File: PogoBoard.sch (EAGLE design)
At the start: 4 parts

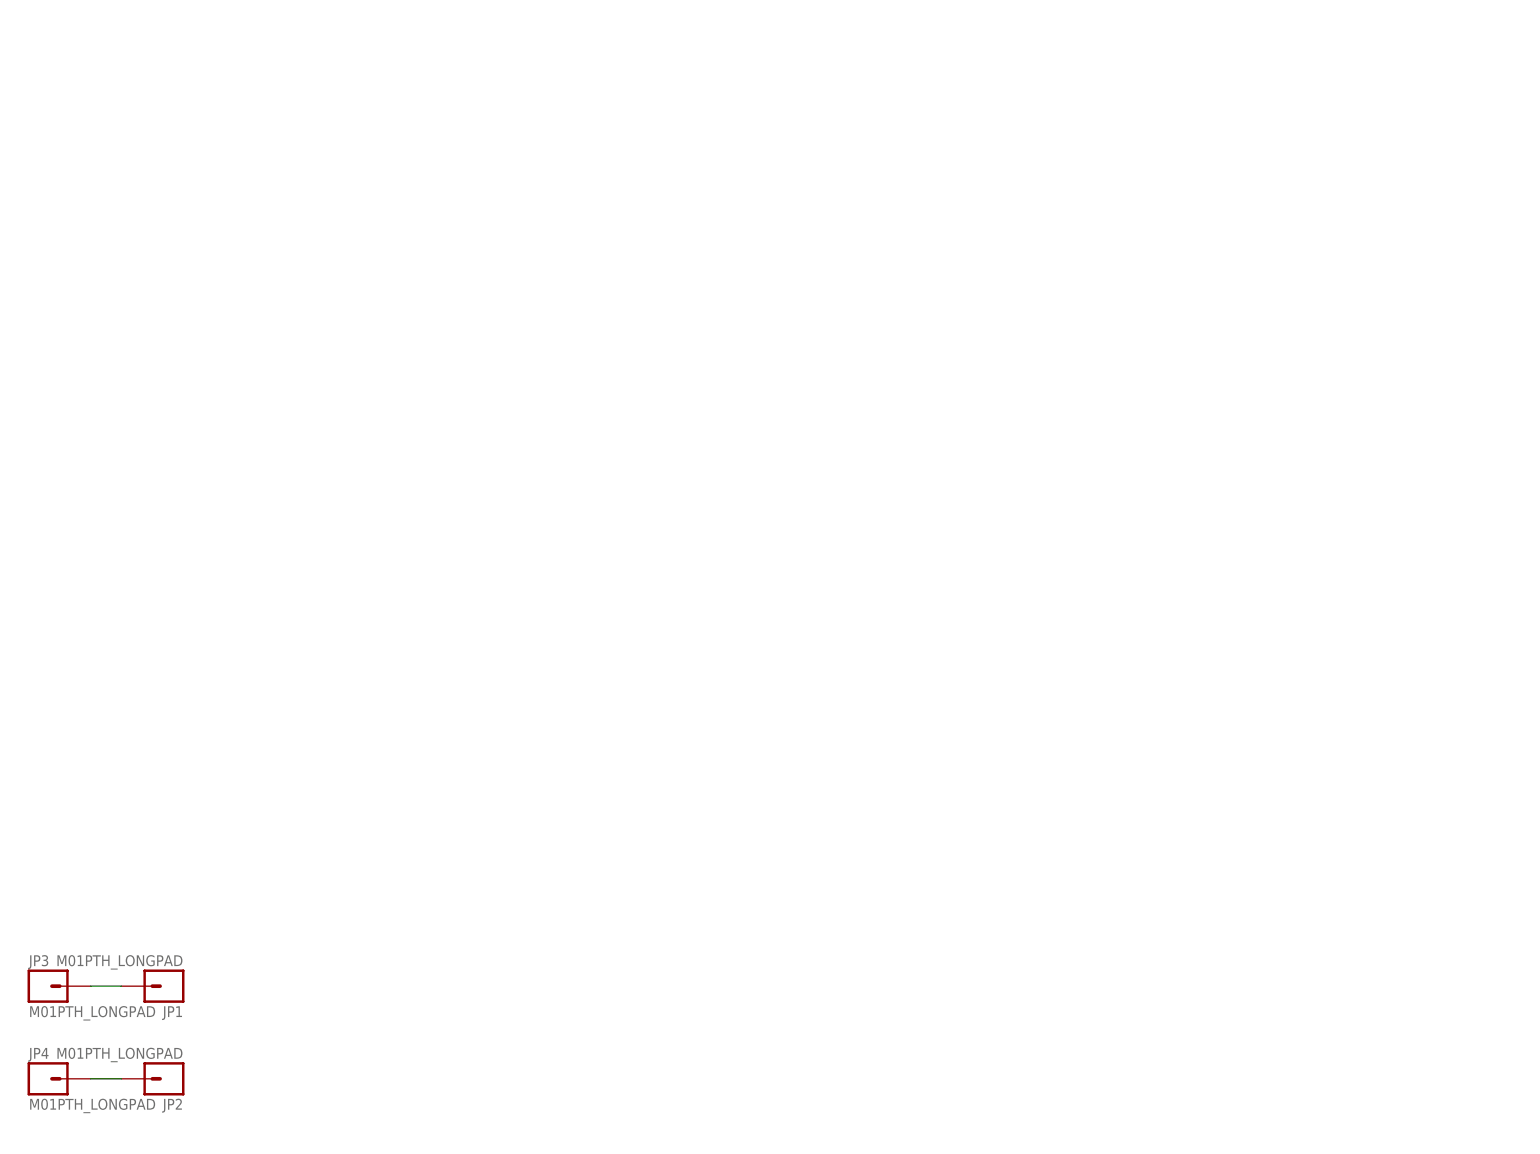
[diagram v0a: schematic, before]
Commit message: Changed pogo board screws to M3
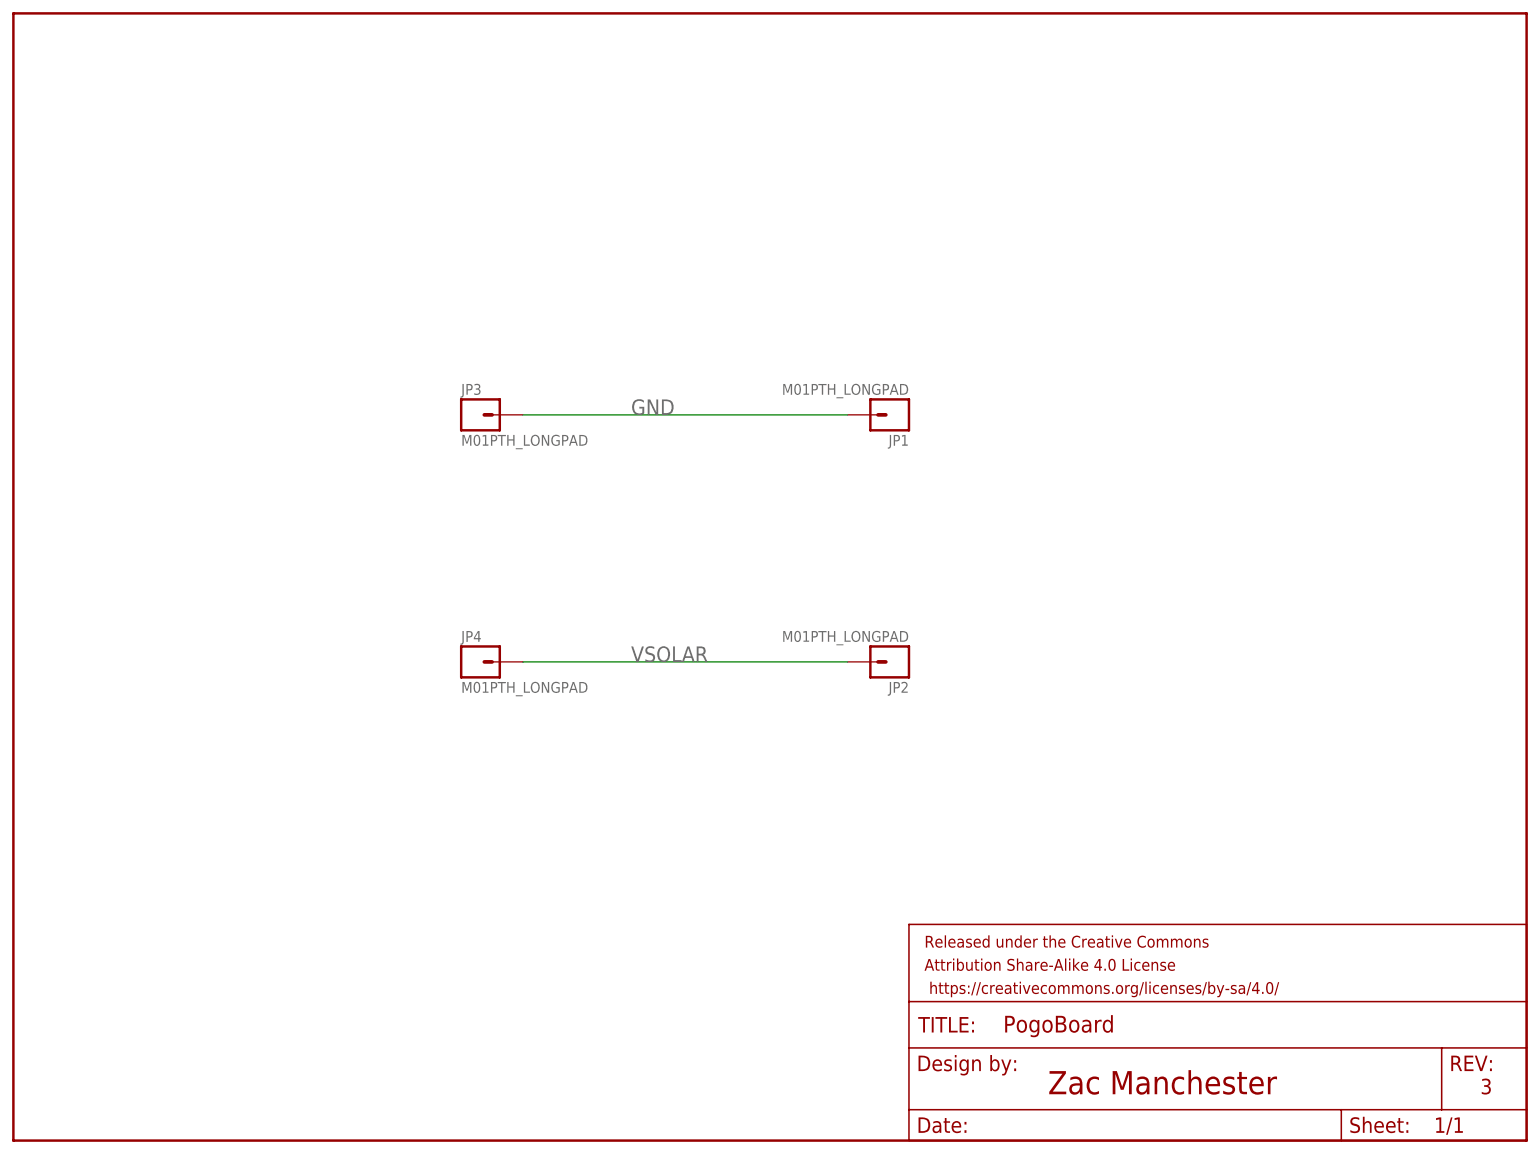
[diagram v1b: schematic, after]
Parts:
- added FRAME1: FRAME-LETTER, SparkFun-Aesthetics:FRAME-LETTER
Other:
- note added: "3"
- note added: "Zac Manchester"
- moved on the sheet: JP1, JP2, JP3, JP4
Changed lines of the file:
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@@
 <layer number="106" name="bPlate" color="7" fill="1" visible="yes" active="yes"/>
 <layer number="107" name="Crop" color="7" fill="1" visible="yes" active="yes"/>
+<layer number="108" name="tplace-old" color="10" fill="1" visible="no" active="yes"/>
+<layer number="109" name="ref-old" color="11" fill="1" visible="no" active="yes"/>
 <layer number="116" name="Patch_BOT" color="9" fill="4" visible="yes" active="yes"/>
 <layer number="121" name="_tsilk" color="7" fill="1" visible="yes" active="yes"/>
 <layer number="122" name="_bsilk" color="7" fill="1" visible="yes" active="yes"/>
+<layer number="125" name="_tNames" color="7" fill="1" visible="yes" active="yes"/>
 <layer number="144" name="Drill_legend" color="7" fill="1" visible="yes" active="yes"/>
 <layer number="151" name="HeatSink" color="7" fill="1" visible="yes" active="yes"/>
+<layer number="199" name="Contour" color="7" fill="1" visible="yes" active="yes"/>
 <layer number="200" name="200bmp" color="1" fill="10" visible="yes" active="yes"/>
 <layer number="201" name="201bmp" color="2" fill="10" visible="yes" active="yes"/>
@@
 <layer number="215" name="215bmp" color="7" fill="1" visible="yes" active="yes"/>
 <layer number="216" name="216bmp" color="7" fill="1" visible="yes" active="yes"/>
+<layer number="217" name="217bmp" color="18" fill="1" visible="no" active="no"/>
+<layer number="218" name="218bmp" color="19" fill="1" visible="no" active="no"/>
+<layer number="219" name="219bmp" color="20" fill="1" visible="no" active="no"/>
+<layer number="220" name="220bmp" color="21" fill="1" visible="no" active="no"/>
+<layer number="221" name="221bmp" color="22" fill="1" visible="no" active="no"/>
+<layer number="222" name="222bmp" color="23" fill="1" visible="no" active="no"/>
+<layer number="223" name="223bmp" color="24" fill="1" visible="no" active="no"/>
+<layer number="224" name="224bmp" color="25" fill="1" visible="no" active="no"/>
 <layer number="250" name="Descript" color="3" fill="1" visible="no" active="no"/>
 <layer number="251" name="SMDround" color="12" fill="11" visible="no" active="no"/>
@@
 <part name="JP3" library="SparkFun" deviceset="M01" device="PTH_LONGPAD"/>
 <part name="JP4" library="SparkFun" deviceset="M01" device="PTH_LONGPAD"/>
+<part name="FRAME1" library="SparkFun-Aesthetics" deviceset="FRAME-LETTER" device=""/>
 </parts>
 <sheets>
 <sheet>
 <plain>
+<text x="170.18" y="7.62" size="3.81" layer="94">Zac Manchester</text>
+<text x="241.3" y="7.62" size="2.54" layer="94">3</text>
 </plain>
 <instances>
-<instance part="JP1" gate="G$1" x="25.4" y="25.4" rot="R180"/>
-<instance part="JP2" gate="G$1" x="25.4" y="10.16" rot="R180"/>
-<instance part="JP3" gate="G$1" x="5.08" y="25.4"/>
-<instance part="JP4" gate="G$1" x="5.08" y="10.16"/>
+<instance part="JP1" gate="G$1" x="144.78" y="119.38" rot="R180"/>
+<instance part="JP2" gate="G$1" x="144.78" y="78.74" rot="R180"/>
+<instance part="JP3" gate="G$1" x="76.2" y="119.38"/>
+<instance part="JP4" gate="G$1" x="76.2" y="78.74"/>
+<instance part="FRAME1" gate="G$1" x="0" y="0"/>
+<instance part="FRAME1" gate="G$2" x="147.32" y="0"/>
 </instances>
 <busses>
@@
 <pinref part="JP3" gate="G$1" pin="1"/>
 <pinref part="JP1" gate="G$1" pin="1"/>
-<wire x1="12.7" y1="25.4" x2="17.78" y2="25.4" width="0.1524" layer="91"/>
+<wire x1="83.82" y1="119.38" x2="137.16" y2="119.38" width="0.1524" layer="91"/>
+<label x="101.6" y="119.38" size="2.54" layer="95"/>
 </segment>
 </net>
@@
 <pinref part="JP4" gate="G$1" pin="1"/>
 <pinref part="JP2" gate="G$1" pin="1"/>
-<wire x1="12.7" y1="10.16" x2="17.78" y2="10.16" width="0.1524" layer="91"/>
+<wire x1="83.82" y1="78.74" x2="137.16" y2="78.74" width="0.1524" layer="91"/>
+<label x="101.6" y="78.74" size="2.54" layer="95"/>
 </segment>
 </net>
